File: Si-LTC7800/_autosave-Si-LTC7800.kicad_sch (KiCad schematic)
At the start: 40 parts, among them J1 TP_VIN1, J2 TP_VOUT1, J3 TP_VOUT2, J4 TP_VOUT2, Q1 BSC100N06LS3_G, Q2 BSC100N06LS3_G, U1 LTC7800HUDC_PBF

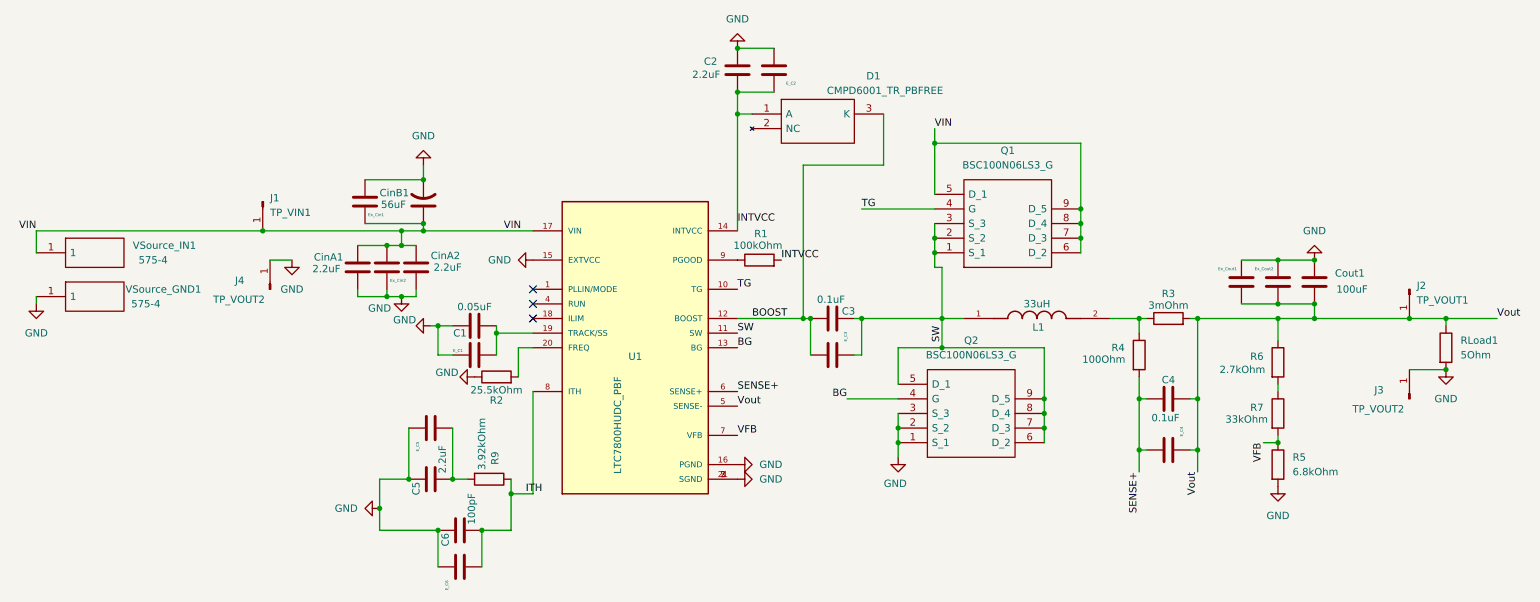
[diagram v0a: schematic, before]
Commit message: Finished draft of GaN PCB
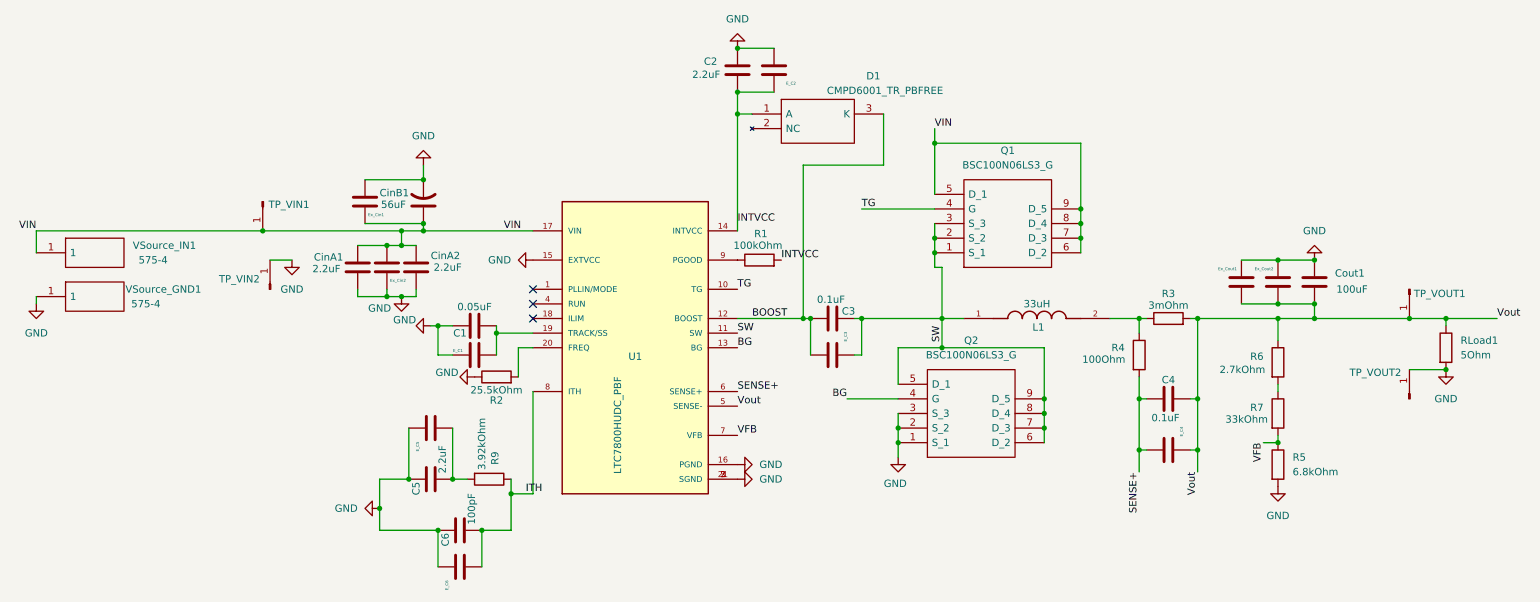
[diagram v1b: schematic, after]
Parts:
- TP_VIN1: renamed from J1; value TP_VIN1 -> ~
- TP_VIN2: renamed from J4; value TP_VOUT2 -> ~
- TP_VOUT1: renamed from J2; value TP_VOUT1 -> ~
- TP_VOUT2: renamed from J3; value TP_VOUT2 -> ~
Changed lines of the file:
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@@
 		(on_board yes)
 		(dnp no)
-		(property "Reference" "J3"
-			(at 252.984 111.506 90)
+		(property "Reference" "TP_VOUT2"
+			(at 248.666 108.458 90)
 			(effects
 				(font
@@
 			)
 		)
-		(property "Value" "TP_VOUT2"
-			(at 249.174 114.808 90)
+		(property "Value" "~"
+			(at 248.92 110.744 90)
 			(effects
 				(font
@@
 			(project "Si-LTC7800"
 				(path "/1cd71796-7ea7-422d-abea-f4fbd11d4a75"
-					(reference "J3")
+					(reference "TP_VOUT2")
 					(unit 1)
 				)
@@
 		(on_board yes)
 		(dnp no)
-		(fields_autoplaced yes)
-		(property "Reference" "J2"
-			(at 260.35 93.3449 90)
+		(property "Reference" "TP_VOUT1"
+			(at 259.842 94.742 90)
 			(effects
 				(font
@@
 			)
 		)
-		(property "Value" "TP_VOUT1"
+		(property "Value" "~"
 			(at 260.35 95.8849 90)
 			(effects
@@
 			(project "Si-LTC7800"
 				(path "/1cd71796-7ea7-422d-abea-f4fbd11d4a75"
-					(reference "J2")
+					(reference "TP_VOUT1")
 					(unit 1)
 				)
@@
 		(on_board yes)
 		(dnp no)
-		(fields_autoplaced yes)
-		(property "Reference" "J1"
-			(at 60.96 78.1049 90)
+		(property "Reference" "TP_VIN1"
+			(at 60.706 79.248 90)
 			(effects
 				(font
@@
 			)
 		)
-		(property "Value" "TP_VIN1"
+		(property "Value" "~"
 			(at 60.96 80.6449 90)
 			(effects
@@
 			(project ""
 				(path "/1cd71796-7ea7-422d-abea-f4fbd11d4a75"
-					(reference "J1")
+					(reference "TP_VIN1")
 					(unit 1)
 				)
@@
 		(on_board yes)
 		(dnp no)
-		(property "Reference" "J4"
-			(at 54.864 92.456 90)
+		(property "Reference" "TP_VIN2"
+			(at 52.07 92.202 90)
 			(effects
 				(font
@@
 			)
 		)
-		(property "Value" "TP_VOUT2"
-			(at 51.054 95.758 90)
+		(property "Value" "~"
+			(at 57.912 93.472 90)
 			(effects
 				(font
@@
 			(project "Si-LTC7800"
 				(path "/1cd71796-7ea7-422d-abea-f4fbd11d4a75"
-					(reference "J4")
+					(reference "TP_VIN2")
 					(unit 1)
 				)
